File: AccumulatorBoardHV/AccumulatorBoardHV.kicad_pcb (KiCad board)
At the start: 2 copper layers, 154.3 x 69.2 mm, 45 parts, among them J1 TS -> GLV Regulator Jumper, J2 To LV Board, J3 Batt Voltage, J4 TS (Switched), J5 IMD TS, J6 To LV Board, J7 Acc LED 1, J8 Acc LED 2, J9 Charger Current, Q1 Q_NMOS_GDS, U1 V110C12E100BL, U2 DK1A1B-12V, U3 RDD08110S3V3, U4 PS2501-4-1, U5 G2RL-1A-E, U6 G2RL-1A-E

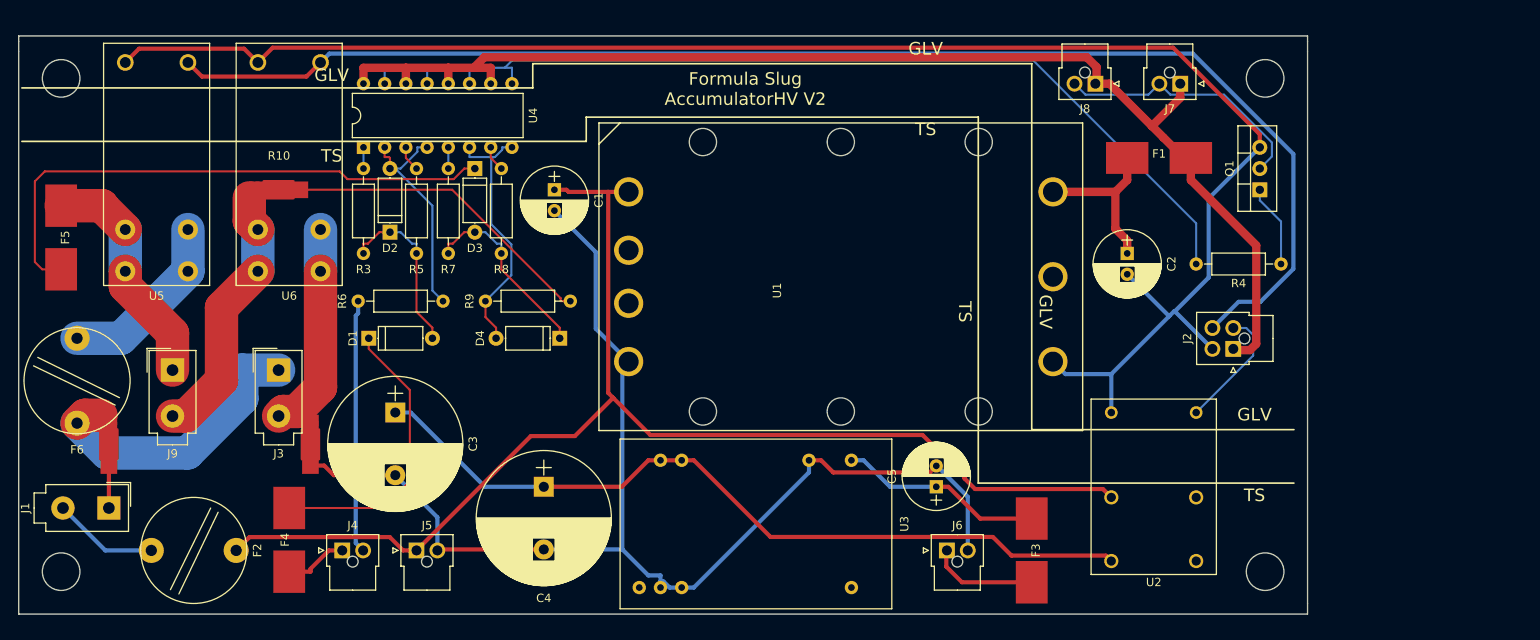
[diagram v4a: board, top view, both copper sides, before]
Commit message: add diodes to relay coils among other things
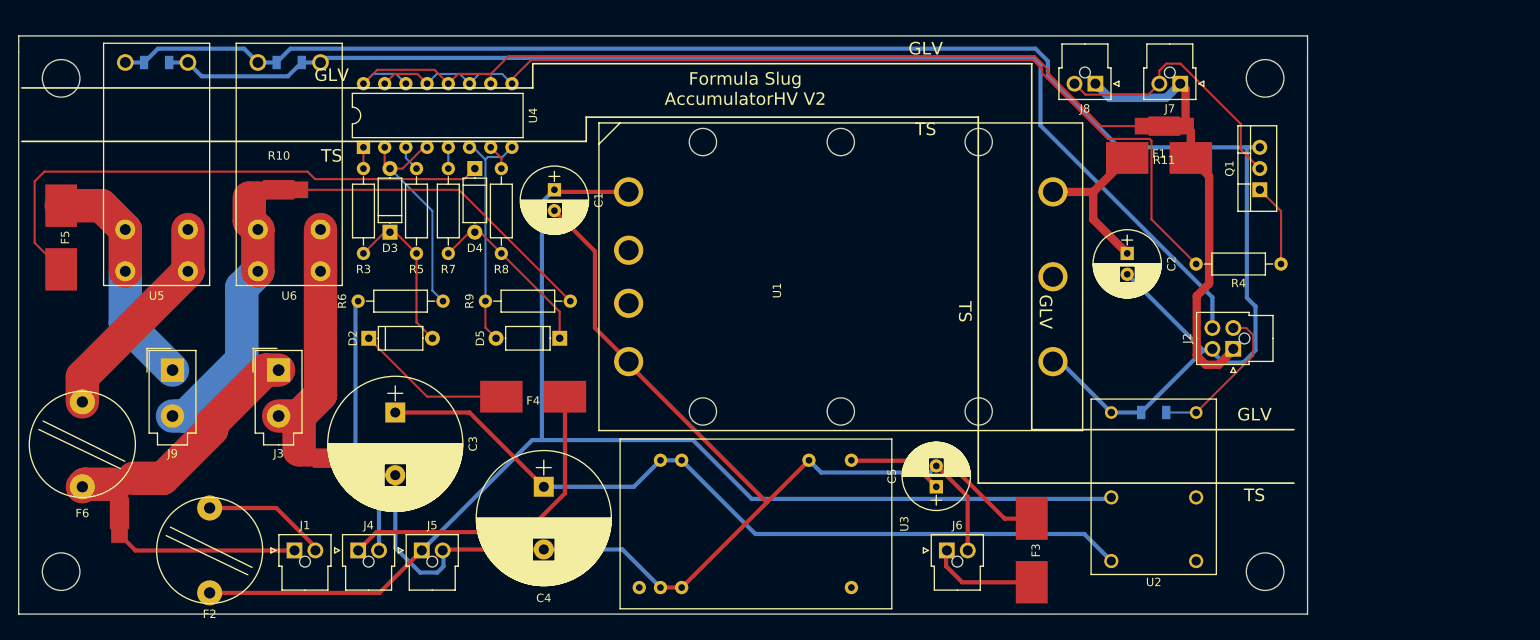
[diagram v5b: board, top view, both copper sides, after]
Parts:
- added D5: 12V Zener, Diodes_THT:D_A-405_P7.62mm_Horizontal, F.Cu at (88.3, 67.3)
- added D6: D, Diodes_SMD:D_1206, B.Cu at (55.9, 34.3)
- added D7: D, Diodes_SMD:D_1206, B.Cu at (40.0, 34.3)
- added R11: 0, FSFootprints:SMDNetTie, F.Cu at (160.7, 41.9)
- D1: value 56V Zener -> D; footprint Diodes_THT:D_A-405_P7.62mm_Horizontal -> Diodes_SMD:D_1206; moved to B.Cu
- D2, D4: value 12V Zener -> 56V Zener
- D3: value 56V Zener -> 12V Zener
- J1: footprint Connectors_Molex:Molex_MiniFit-JR-5556-02A_2x01x4.20mm_Straight -> Connectors_Molex:Molex_NanoFit_1x02x2.50mm_Straight
- moved D1 94.4 mm to (159.4, 76.2), turned to 180 degrees
- moved F4 33.9 mm to (85.1, 74.3), turned to 0 degrees
- moved J1 22.8 mm to (56.5, 92.7), turned to 0 degrees
- moved D4 22.7 mm to (78.1, 47.0), turned to 270 degrees
- moved D2 13.0 mm to (65.4, 67.3), turned to 0 degrees
- moved D3 12.7 mm to (67.9, 54.6), turned to 90 degrees
- moved R1 8.35 mm to (35.6, 88.3)
- moved F6 7.65 mm to (31.1, 85.1)
- moved F2 5.99 mm to (46.4, 97.8), turned to 90 degrees
- moved R2 2.72 mm to (60.6, 81.7), turned to 180 degrees
- moved J4 1.91 mm to (64.1, 92.7)
- moved J5 0.63 mm to (71.8, 92.7)
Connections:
- D1 pad 1: Net-(D1-Pad1) -> /12V
- D1 pad 2: Net-(D1-Pad2) -> GND
- D2 pad 1: Net-(D1-Pad2) -> Net-(D2-Pad1)
- D3 pad 1: Net-(D3-Pad1) -> Net-(D2-Pad2)
- D4 pad 1: Net-(D3-Pad2) -> Net-(D4-Pad1)
- F4 pad 1: Net-(D1-Pad1) -> Net-(D2-Pad1)
- F5 pad 1: Net-(D3-Pad1) -> Net-(D4-Pad1)
- R3 pad 2: Net-(D1-Pad2) -> Net-(D2-Pad2)
- R5 pad 2: Net-(D1-Pad2) -> Net-(D2-Pad2)
- R6 pad 1: Net-(D2-Pad2) -> Net-(D3-Pad2)
- R7 pad 2: Net-(D3-Pad2) -> Net-(D4-Pad2)
- R8 pad 2: Net-(D3-Pad2) -> Net-(D4-Pad2)
- R9 pad 1: Net-(D4-Pad2) -> Net-(D5-Pad2)
- U4 pad 10: /12V_SRC -> /12V_SRC_OPTO
- U4 pad 12: /12V_SRC -> /12V_SRC_OPTO
- U4 pad 14: /12V_SRC -> /12V_SRC_OPTO
- U4 pad 16: /12V_SRC -> /12V_SRC_OPTO
- U4 pad 2: Net-(D2-Pad2) -> Net-(D3-Pad2)
- U4 pad 4: Net-(D2-Pad2) -> Net-(D3-Pad2)
- U4 pad 6: Net-(D4-Pad2) -> Net-(D5-Pad2)
- U4 pad 8: Net-(D4-Pad2) -> Net-(D5-Pad2)
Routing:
- net /12V_SRC_OPTO: track 0.00 -> 107.0 mm
- net /12V_SRC: track 150.7 -> 51.9 mm
- net Net-(D3-Pad1): track 67.2 -> 0.00 mm
- net Net-(D4-Pad1): track 0.00 -> 65.9 mm
- net Net-(D1-Pad1): track 34.9 -> 0.00 mm
- net /TS+: track 7.60 -> 39.2 mm
- net Net-(D5-Pad2): track 0.00 -> 28.2 mm
- net Net-(D1-Pad2): track 20.8 -> 0.00 mm
- net /AIRS_FINAL_CHARGER: track 165.5 -> 146.3 mm
- net Net-(D2-Pad1): track 0.00 -> 18.8 mm
- net /BATT+_DIRECT: track 5.08 -> 21.7 mm
- net Net-(D4-Pad2): track 31.5 -> 21.5 mm
- net GND: track 204.0 -> 212.8 mm
- net Net-(D2-Pad2): track 27.2 -> 19.4 mm
- net /BATT+_CHARGER: track 36.3 -> 30.5 mm
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
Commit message: Update 60V circuit some more, on both boards
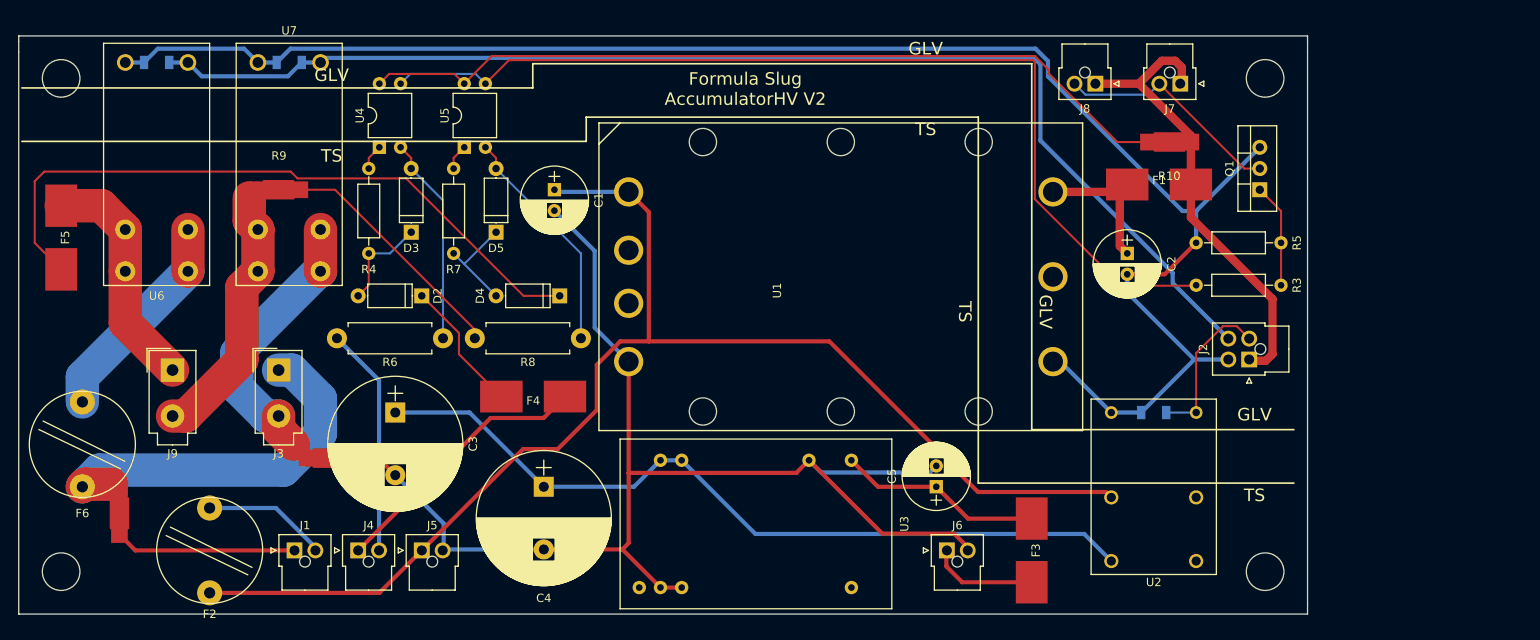
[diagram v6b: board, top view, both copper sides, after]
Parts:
- removed R11: 0, FSFootprints:SMDNetTie
- added U7: G2RL-1A-E, FSFootprints:G2RL-1A-E, F.Cu at (55.9, 34.3)
- R3: value 1.2k -> 100
- R4: value 100 -> 1.2k
- R5: value 1.2k -> 100k
- R6: value 1.5k -> 10k; footprint Resistors_THT:R_Axial_DIN0207_L6.3mm_D2.5mm_P10.16mm_Horizontal -> Resistors_THT:R_Axial_DIN0411_L9.9mm_D3.6mm_P12.70mm_Horizontal
- R8: value 1.2k -> 10k; footprint Resistors_THT:R_Axial_DIN0207_L6.3mm_D2.5mm_P10.16mm_Horizontal -> Resistors_THT:R_Axial_DIN0411_L9.9mm_D3.6mm_P12.70mm_Horizontal
- R9: value 1.5k -> 0; footprint Resistors_THT:R_Axial_DIN0207_L6.3mm_D2.5mm_P10.16mm_Horizontal -> FSFootprints:SMDNetTie
- U4: value PS2501-4-1 -> PS2501-1; footprint Housings_DIP:DIP-16_W7.62mm -> Housings_DIP:DIP-4_W7.62mm
- U5: value G2RL-1A-E -> PS2501-1; footprint FSFootprints:G2RL-1A-E -> Housings_DIP:DIP-4_W7.62mm
- moved R3 110.7 mm to (174.6, 61.0), turned to 180 degrees
- moved R4 109.8 mm to (65.4, 47.0), turned to 270 degrees
- moved R10 106.8 mm to (161.3, 43.8), turned to 0 degrees
- moved R5 93.8 mm to (164.5, 55.9), turned to 0 degrees
- moved U5 38.2 mm to (76.8, 44.5), turned to 90 degrees
- moved R9 28.1 mm to (54.6, 49.5), turned to 180 degrees
- moved R8 22.4 mm to (90.8, 67.3), turned to 180 degrees
- moved D4 18.3 mm to (88.3, 62.2), turned to 180 degrees
- moved U6 15.9 mm to (40.0, 34.3)
- moved D5 14.8 mm to (80.6, 54.6), turned to 90 degrees
- moved D2 8.13 mm to (71.8, 62.2), turned to 180 degrees
- moved R6 4.45 mm to (74.3, 67.3)
- moved F1 3.18 mm to (160.0, 48.9)
- moved D3 2.54 mm to (70.5, 54.6)
- moved J2 2.29 mm to (170.8, 69.8)
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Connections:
- R10 pad 1: Net-(R10-Pad1) -> /12V_SRC_OPTO
- R10 pad 2: /CHARGER- -> /12V_SRC
- R3 pad 1: Net-(R3-Pad1) -> Net-(Q1-Pad1)
- R3 pad 2: Net-(D2-Pad2) -> /12V_INDICATOR_CTRL
- R4 pad 1: Net-(Q1-Pad1) -> Net-(R4-Pad1)
- R4 pad 2: /12V_INDICATOR_CTRL -> Net-(D2-Pad2)
- R5 pad 1: Net-(R5-Pad1) -> GND
- R5 pad 2: Net-(D2-Pad2) -> Net-(Q1-Pad1)
- R8 pad 1: Net-(R8-Pad1) -> Net-(D5-Pad2)
- R8 pad 2: Net-(D4-Pad2) -> Net-(R8-Pad2)
- R9 pad 1: Net-(D5-Pad2) -> Net-(R8-Pad2)
- R9 pad 2: Net-(R10-Pad1) -> /CHARGER-
- U4 pad 1: Net-(R3-Pad1) -> Net-(R4-Pad1)
- U4 pad 3: Net-(R5-Pad1) -> /12V_INDICATOR_CTRL
- U4 pad 4: Net-(D3-Pad2) -> /12V_SRC_OPTO
- U5 pad 1: /AIRS_FINAL_CHARGER -> Net-(R7-Pad1)
- U5 pad 3: /BATT+_CHGFUSED -> /12V_INDICATOR_CTRL
- U5 pad 4: /BATT+_CHGFUSED -> /12V_SRC_OPTO
- U6 pad 3: /BATT-_CHARGER -> /BATT+_CHGFUSED
- U6 pad 4: /BATT-_CHARGER -> /BATT+_CHGFUSED
- U6 pad 5: /CHARGER- -> /CHARGER+
- U6 pad 6: /CHARGER- -> /CHARGER+
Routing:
- net Net-(R10-Pad1): track 37.9 -> 0.00 mm
- net Net-(R8-Pad2): track 0.00 -> 28.9 mm
- net /BATT+_CHARGER: track 30.5 -> 46.7 mm
- net Net-(D4-Pad1): track 65.9 -> 81.4 mm
- net GND: track 212.8 -> 203.5 mm
- net Net-(D4-Pad2): track 21.5 -> 12.6 mm
- net /12V_SRC_OPTO: track 107.0 -> 98.9 mm
- net Net-(D2-Pad2): track 19.4 -> 11.7 mm
- net /TS+: track 39.2 -> 32.4 mm
- net /BATT-: track 149.7 -> 154.8 mm
- net /BATT-_CHARGER: track 31.3 -> 36.1 mm
- net /12V_INDICATOR: track 32.2 -> 27.5 mm
- net /3.3V_TS_PRE: track 29.0 -> 24.5 mm
- net /12V_SRC: track 51.9 -> 56.0 mm
- net /TS-: track 31.1 -> 27.5 mm
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
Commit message: move connectors to assist in battery packaging
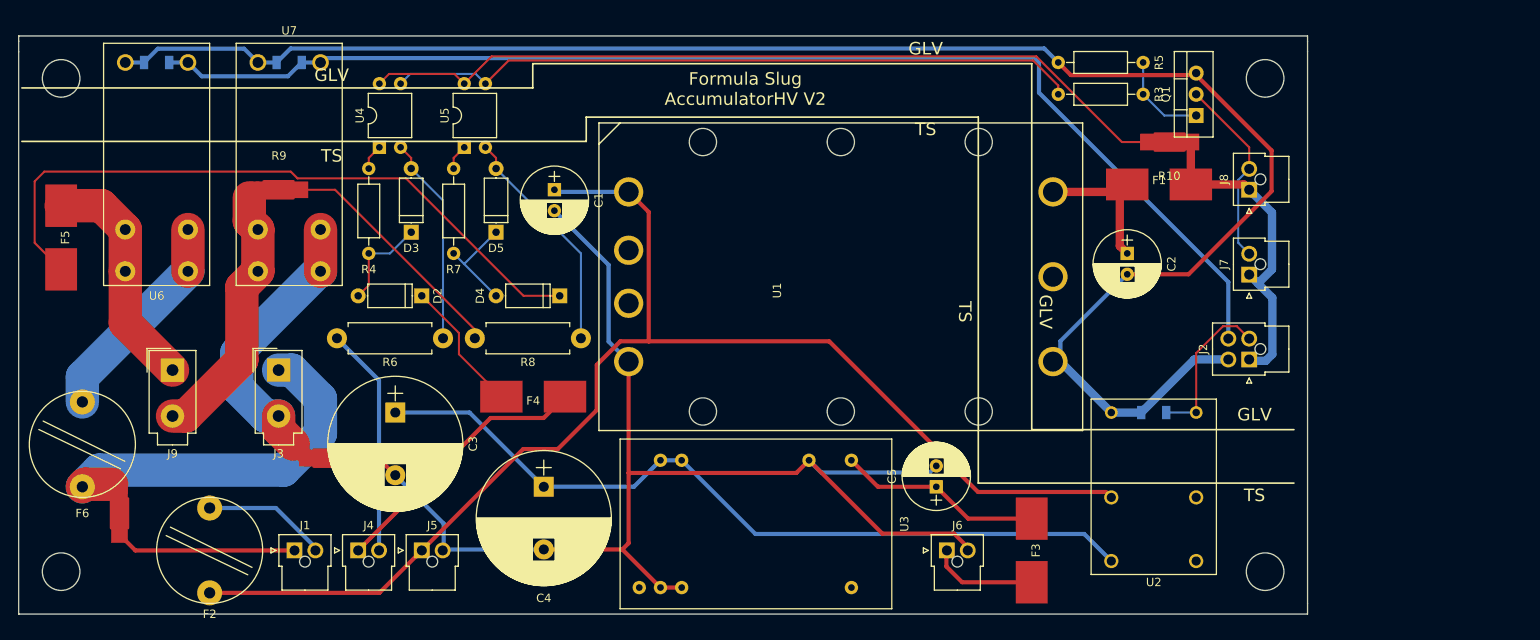
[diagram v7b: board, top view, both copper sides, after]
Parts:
- moved R3 28.2 mm to (158.1, 38.1)
- moved R5 27.2 mm to (148.0, 34.3)
- moved J7 24.3 mm to (170.8, 59.7), turned to 90 degrees
- moved J8 22.4 mm to (170.8, 49.5), turned to 90 degrees
- moved Q1 11.7 mm to (164.5, 40.6)
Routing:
- net /12V_INDICATOR_CTRL: track 118.2 -> 83.1 mm
- net /12V_SRC: track 56.0 -> 39.2 mm
- net GND: track 203.5 -> 210.8 mm
- net /12V_INDICATOR: track 27.5 -> 22.8 mm
- net Net-(Q1-Pad1): track 12.5 -> 11.2 mm

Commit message: hopefully finalize PCBs for send to manufacturing
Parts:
- R1: moved to B.Cu
- moved R9 30.5 mm to (47.4, 79.1), turned to 90 degrees
- moved D2 5.08 mm to (76.8, 62.2)
- moved D6 3.18 mm to (52.7, 34.3)
- moved U7 3.18 mm to (52.7, 34.3)
- moved U4 2.54 mm to (69.2, 44.5)
- moved R4 2.54 mm to (67.9, 47.0)
- moved F5 1.42 mm to (27.3, 55.9), turned to 270 degrees
- moved D7 1.27 mm to (38.7, 34.3)
- moved U6 1.27 mm to (38.7, 34.3)
- moved D3 1.27 mm to (71.8, 54.6)
- moved R7 1.27 mm to (76.8, 47.0)
- moved R1 0.76 mm to (36.3, 88.3)
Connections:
- net Net-(D2-Pad1) renamed /TS+_F
- net Net-(D4-Pad1) renamed /CHARGER+_F
- net Net-(R8-Pad2) renamed /CHARGER-_60
- U6 pad 4: /BATT+_CHGFUSED -> /CHARGER+
- U6 pad 6: /CHARGER+ -> /BATT+_CHGFUSED
- U7 pad 4: /BATT-_CHARGER -> /CHARGER-
- U7 pad 6: /CHARGER- -> /BATT-_CHARGER
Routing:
- net /CHARGER-_60: track 28.9 -> 47.9 mm
- net /CHARGER+_F: track 81.4 -> 65.9 mm
- net /BATT-_CHARGER: track 36.1 -> 50.3 mm
- net /BATT+_CHARGER: track 46.7 -> 33.3 mm
- net /BATT-: track 154.8 -> 142.2 mm
- net /BATT+_CHGFUSED: track 25.9 -> 33.5 mm
- net /3.3V_TS_PRE: track 24.5 -> 29.0 mm
- net /BATT+: track 159.4 -> 163.6 mm
- net GND: track 210.8 -> 214.3 mm
- net /12V_SRC_OPTO: track 98.6 -> 96.1 mm
- net /12V_INDICATOR_CTRL: track 83.1 -> 80.6 mm
- net /CHARGER-: track 33.1 -> 30.9 mm
- net /TS+_F: track 16.0 -> 13.9 mm
- net Net-(D2-Pad2): track 11.7 -> 9.94 mm
- net Net-(D4-Pad2): track 12.6 -> 11.0 mm
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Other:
- net class HV added: clearance 0.6, trace_width 0.25, via_dia 0.8, via_drill 0.4
